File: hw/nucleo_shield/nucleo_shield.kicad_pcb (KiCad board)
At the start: 2 copper layers, 151 x 90.9 mm, 69 parts, among them CN101 Nucleo-F411RE-CN10, CN71 Nucleo-F411RE-CN7, P1 CONN_INH1, P10 CONN_OUTH1, P11 CONN_OUTH2, P12 CONN_RS485_OUT, P13 CONN_RS485_IN, P15 CONN_EXT2, P16 CONN_EXTI2C, P18 CONN_1WIRE, P19 CONN_EXT_SPI, P2 CONN_OUT3, P20 CON_BME, P3 POWER_24V_CON, P4 POWER_CON, P5 CONN_INH2, P6 ETH_CONN, P7 CONN_LCD_SD, P8 CONN_OUT4, P9 CONN_SCT, U1 74HC595, U10 ULN2803, U11 74HC595, U12 74HC595, U14 PCF8574A, U2 74HC595, U3 LTV-847, U4 LTV-847, U5 LTV-847, U6 LTV-847, U7 PCF8574A, U8 PCF8574A, U9 ULN2803

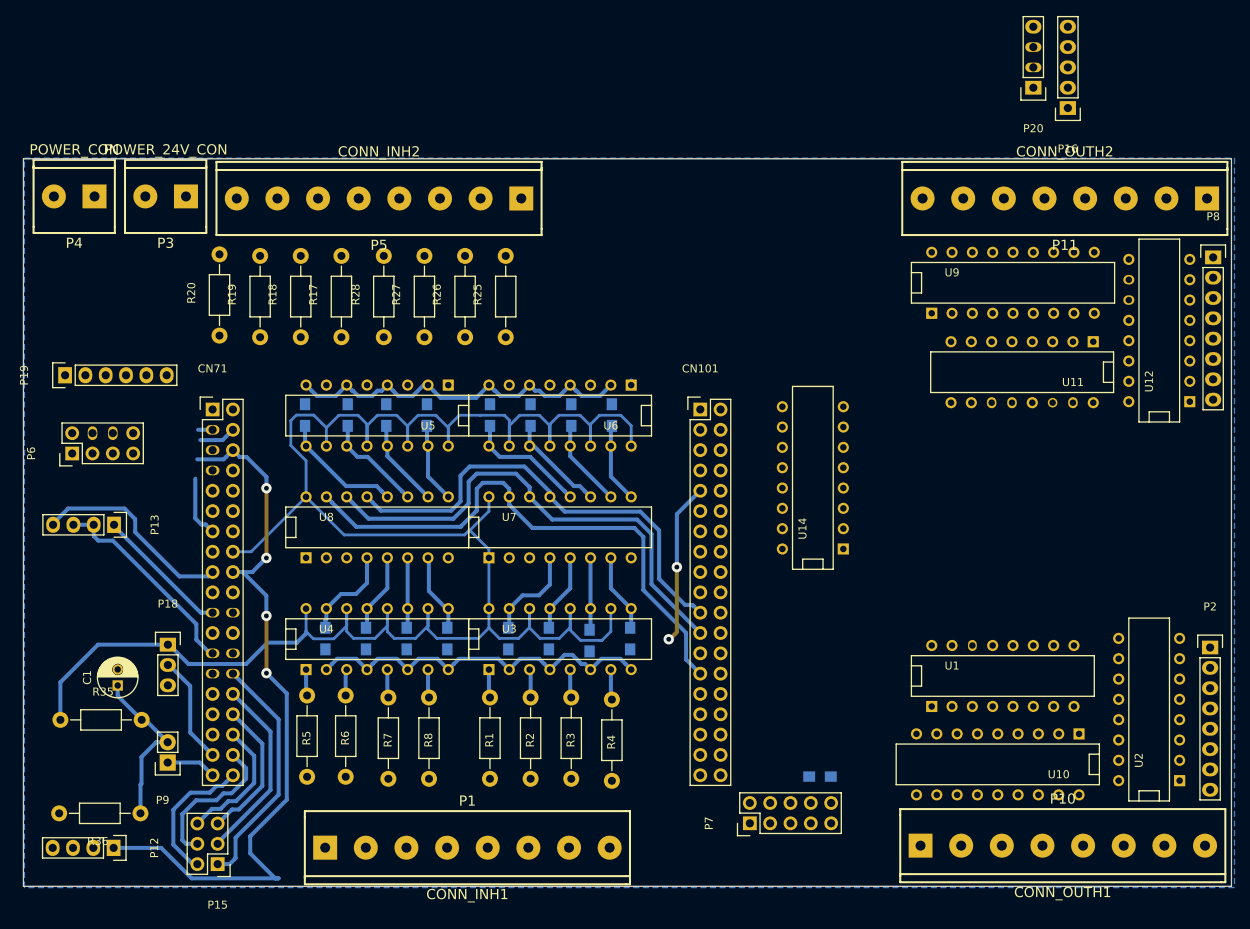
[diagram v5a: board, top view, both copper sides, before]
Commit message: HW: rework of nucleo shield to add more IOs
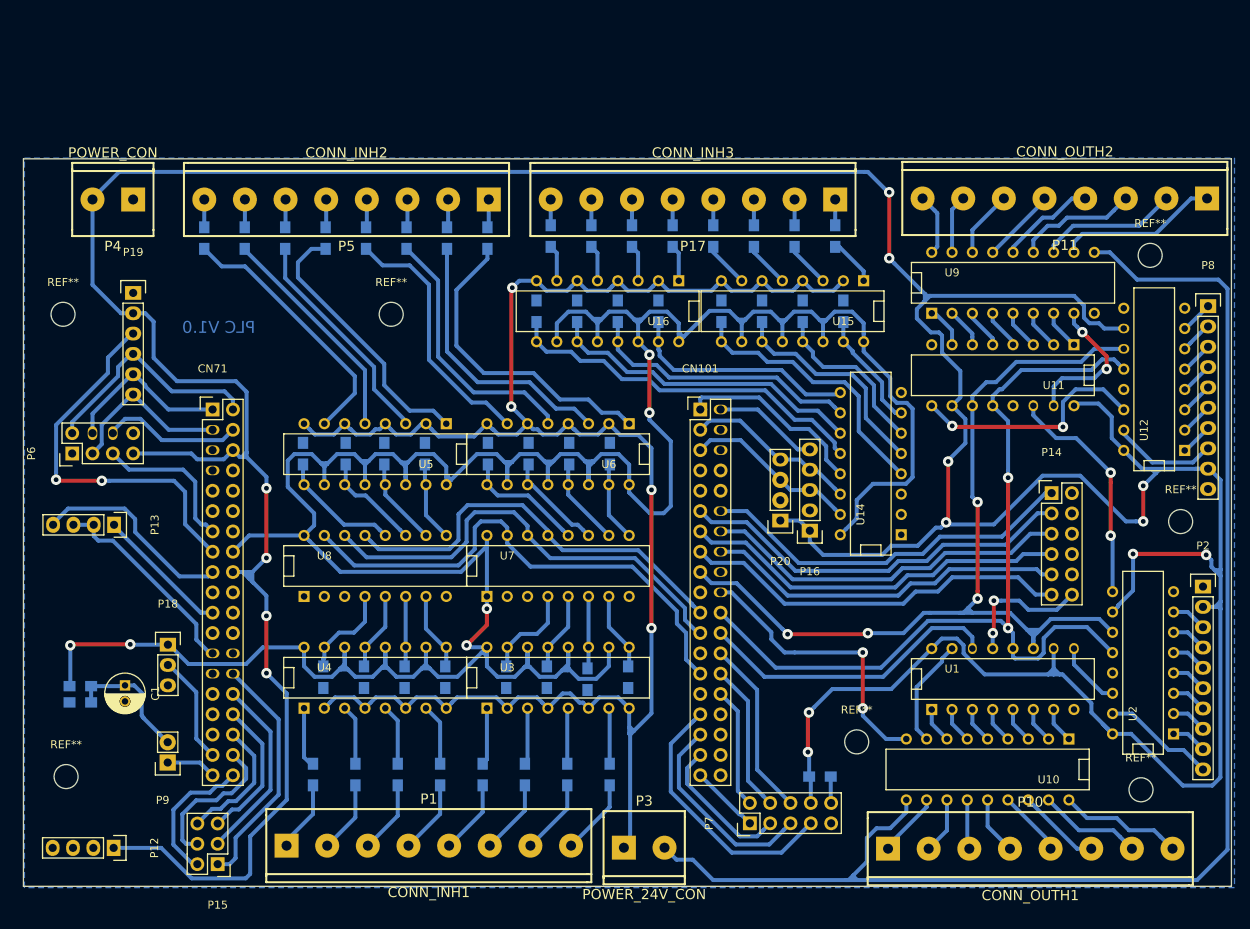
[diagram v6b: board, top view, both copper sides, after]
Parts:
- added P14: CONN_02X06, Pin_Headers:Pin_Header_Straight_2x06, F.Cu at (223.6, 99.8)
- added P17: CONN_INH3, w_conn_screw:mors_8p, F.Cu at (178.8, 63.1)
- added R34: R, Resistors_SMD:R_0805_HandSoldering, B.Cu at (196.6, 67.7)
- added R37: R, Resistors_SMD:R_0805_HandSoldering, B.Cu at (191.5, 67.7)
- added R38: R, Resistors_SMD:R_0805_HandSoldering, B.Cu at (186.4, 67.7)
- added R39: R, Resistors_SMD:R_0805_HandSoldering, B.Cu at (181.4, 67.7)
- added R40: R, Resistors_SMD:R_0805_HandSoldering, B.Cu at (176.3, 67.7)
- added R41: R, Resistors_SMD:R_0805_HandSoldering, B.Cu at (171.2, 67.7)
- added R42: R, Resistors_SMD:R_0805_HandSoldering, B.Cu at (166.1, 67.7)
- added R43: R, Resistors_SMD:R_0805_HandSoldering, B.Cu at (161.0, 67.7)
- added R44: R, Resistors_SMD:R_0805_HandSoldering, B.Cu at (182.4, 77.1)
- added R45: R, Resistors_SMD:R_0805_HandSoldering, B.Cu at (159.3, 77.1)
- added R46: R, Resistors_SMD:R_0805_HandSoldering, B.Cu at (187.5, 77.1)
- added R47: R, Resistors_SMD:R_0805_HandSoldering, B.Cu at (164.3, 77.1)
- added R48: R, Resistors_SMD:R_0805_HandSoldering, B.Cu at (192.5, 77.1)
- added R49: R, Resistors_SMD:R_0805_HandSoldering, B.Cu at (169.4, 77.1)
- added R50: R, Resistors_SMD:R_0805_HandSoldering, B.Cu at (197.6, 77.1)
- added R51: R, Resistors_SMD:R_0805_HandSoldering, B.Cu at (174.5, 77.1)
- added REF**: MountingHole_3mm, Mounting_Holes:MountingHole_3mm, F.Cu at (236.0, 70.1)
- added REF**: MountingHole_3mm, Mounting_Holes:MountingHole_3mm, F.Cu at (100.5, 135.3)
- added REF**: MountingHole_3mm, Mounting_Holes:MountingHole_3mm, F.Cu at (141.1, 77.5)
- added REF**: MountingHole_3mm, Mounting_Holes:MountingHole_3mm, F.Cu at (100.1, 77.5)
- added REF**: MountingHole_3mm, Mounting_Holes:MountingHole_3mm, F.Cu at (239.8, 103.4)
- added REF**: MountingHole_3mm, Mounting_Holes:MountingHole_3mm, F.Cu at (234.8, 136.9)
- added REF**: MountingHole_3mm, Mounting_Holes:MountingHole_3mm, F.Cu at (199.3, 130.9)
- added U15: LTV-847, Housings_DIP:DIP-16__300, F.Cu at (191.3, 77.1)
- added U16: LTV-847, Housings_DIP:DIP-16__300, F.Cu at (168.1, 77.1)
- P2, P8: footprint Pin_Headers:Pin_Header_Straight_1x08 -> Pin_Headers:Pin_Header_Straight_1x10
- R1, R17, R18, R19, R2, R20, R25, R26, R27, R28, R3, R35, R36, R4, R5, R6, R7, R8: footprint Resistors_ThroughHole:Resistor_Horizontal_RM10mm -> Resistors_SMD:R_0805_HandSoldering; moved to B.Cu
- moved P3 101.0 mm to (172.7, 144.1), turned to 0 degrees
- moved P20 62.7 mm to (189.7, 103.3)
- moved P16 61.9 mm to (193.4, 104.5)
- moved R36 15.8 mm to (102.2, 126.0)
- moved P19 13.4 mm to (108.8, 74.8), turned to 0 degrees
- moved R25 12.6 mm to (153.1, 67.9)
- moved R26 12.6 mm to (148.1, 67.9)
- moved R27 12.6 mm to (143.0, 67.9)
- moved R28 12.6 mm to (138.0, 67.9)
- moved P2 7.67 mm to (242.6, 111.5)
- moved R17 7.57 mm to (132.9, 67.9)
- moved R18 7.56 mm to (127.8, 67.9)
- moved R19 7.56 mm to (122.8, 67.9)
- moved U14 7.45 mm to (201.0, 96.1)
- moved R20 7.36 mm to (117.7, 67.9)
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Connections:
- CN101 pad 1: I2C_GPIO -> I2C1_GPIO
- CN101 pad 10: Net-(CN101-Pad10) -> (no net)
- CN101 pad 11: Net-(CN101-Pad11) -> /PA5
- CN101 pad 12: SRLatch2 -> /PA12
- CN101 pad 13: Net-(CN101-Pad13) -> /PA6
- CN101 pad 14: SRDATA2 -> /PA11
- CN101 pad 15: Net-(CN101-Pad15) -> /PA7
- CN101 pad 16: SRCLK -> /PB12
- CN101 pad 17: Net-(CN101-Pad17) -> SRCLK
- CN101 pad 18: Net-(CN101-Pad18) -> (no net)
- CN101 pad 19: Net-(CN101-Pad19) -> (no net)
- CN101 pad 2: I2C1_GPIO -> I2C_GPIO
- CN101 pad 25: Net-(CN101-Pad25) -> (no net)
- CN101 pad 29: Net-(CN101-Pad29) -> (no net)
- CN101 pad 32: Net-(CN101-Pad32) -> (no net)
- CN101 pad 34: Net-(CN101-Pad34) -> (no net)
- CN101 pad 36: Net-(CN101-Pad36) -> (no net)
- CN101 pad 38: Net-(CN101-Pad38) -> (no net)
- CN101 pad 4: Net-(CN101-Pad4) -> (no net)
- CN101 pad 6: SRCLK2 -> (no net)
- CN101 pad 7: Net-(CN101-Pad7) -> (no net)
- CN101 pad 8: Net-(CN101-Pad8) -> (no net)
- CN71 pad 10: Net-(CN71-Pad10) -> (no net)
- CN71 pad 11: Net-(CN71-Pad11) -> (no net)
- CN71 pad 12: Net-(CN71-Pad12) -> (no net)
- CN71 pad 14: Net-(CN71-Pad14) -> (no net)
- CN71 pad 23: Net-(CN71-Pad23) -> (no net)
- CN71 pad 24: Net-(CN71-Pad24) -> (no net)
- CN71 pad 26: Net-(CN71-Pad26) -> (no net)
- CN71 pad 27: Net-(CN71-Pad27) -> (no net)
- CN71 pad 29: Net-(CN71-Pad29) -> (no net)
- CN71 pad 31: Net-(CN71-Pad31) -> (no net)
- CN71 pad 33: Net-(CN71-Pad33) -> (no net)
- CN71 pad 5: +3V3 -> (no net)
- CN71 pad 7: Net-(CN71-Pad7) -> (no net)
- CN71 pad 9: Net-(CN71-Pad9) -> (no net)
- P12 pad 2: Net-(P12-Pad2) -> (no net)
- P12 pad 3: Net-(P12-Pad3) -> (no net)
- P16 pad 3: I2C_GPIO -> I2C1_SDA
- P16 pad 5: I2C1_SDA -> I2C_GPIO
- P2 pad 1: out24 -> GND
- P2 pad 2: out23 -> +5V
- P2 pad 3: out22 -> out24
- P2 pad 4: out21 -> out23
- P2 pad 5: out20 -> out22
- P2 pad 6: out19 -> out21
- P2 pad 7: out18 -> out20
- P2 pad 8: out17 -> out19
- P20 pad 3: I2C1_SCL -> I2C1_SDA
- P20 pad 4: I2C1_SDA -> I2C1_SCL
- P6 pad 8: GND -> (no net)
- U11 pad 11: SRLatch2 -> SRCLK
- U11 pad 12: SRCLK2 -> SRLatch
- U11 pad 14: SRDATA2 -> Net-(U11-Pad14)
- U12 pad 11: SRLatch2 -> SRCLK
- U12 pad 12: SRCLK2 -> SRLatch
- U12 pad 9: Net-(U12-Pad9) -> (no net)
- U14 pad 1: +3V3 -> GND
- U14 pad 10: Net-(U14-Pad10) -> in22
- U14 pad 11: Net-(U14-Pad11) -> in23
- U14 pad 12: Net-(U14-Pad12) -> in24
- U14 pad 4: Net-(U14-Pad4) -> in17
- U14 pad 5: Net-(U14-Pad5) -> in18
- U14 pad 6: Net-(U14-Pad6) -> in19
- U14 pad 7: Net-(U14-Pad7) -> in20
- U14 pad 9: Net-(U14-Pad9) -> in21
- U2 pad 11: Net-(U2-Pad11) -> SRCLK
- U2 pad 12: Net-(U2-Pad12) -> SRLatch
- U2 pad 9: Net-(U2-Pad9) -> Net-(U11-Pad14)
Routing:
- net +5V: track 92.0 -> 555.6 mm, vias 4 -> 14
- net +24V: track 0.00 -> 177.4 mm
- net +3V3: track 266.5 -> 406.9 mm, vias 0 -> 6
- net GND_24V: track 92.5 -> 221.4 mm, vias 0 -> 4
- net SRCLK: track 0.00 -> 115.3 mm, vias 0 -> 4
- net SRLatch: track 0.00 -> 110.9 mm, vias 0 -> 2
- net /PA5: track 0.00 -> 49.9 mm
- net /PA7: track 0.00 -> 48.9 mm
- net /PA6: track 0.00 -> 48.5 mm
- net EXT_SPI_SS: track 0.00 -> 48.0 mm, vias 0 -> 2
- net /PA12: track 0.00 -> 47.7 mm
- net in24: track 0.00 -> 46.6 mm
- net /PA11: track 0.00 -> 46.2 mm
- net /PB12: track 0.00 -> 45.3 mm
- net in23: track 0.00 -> 40.1 mm
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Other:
- board text added: "PLC V1.0"

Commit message: HW: add another header for i2c
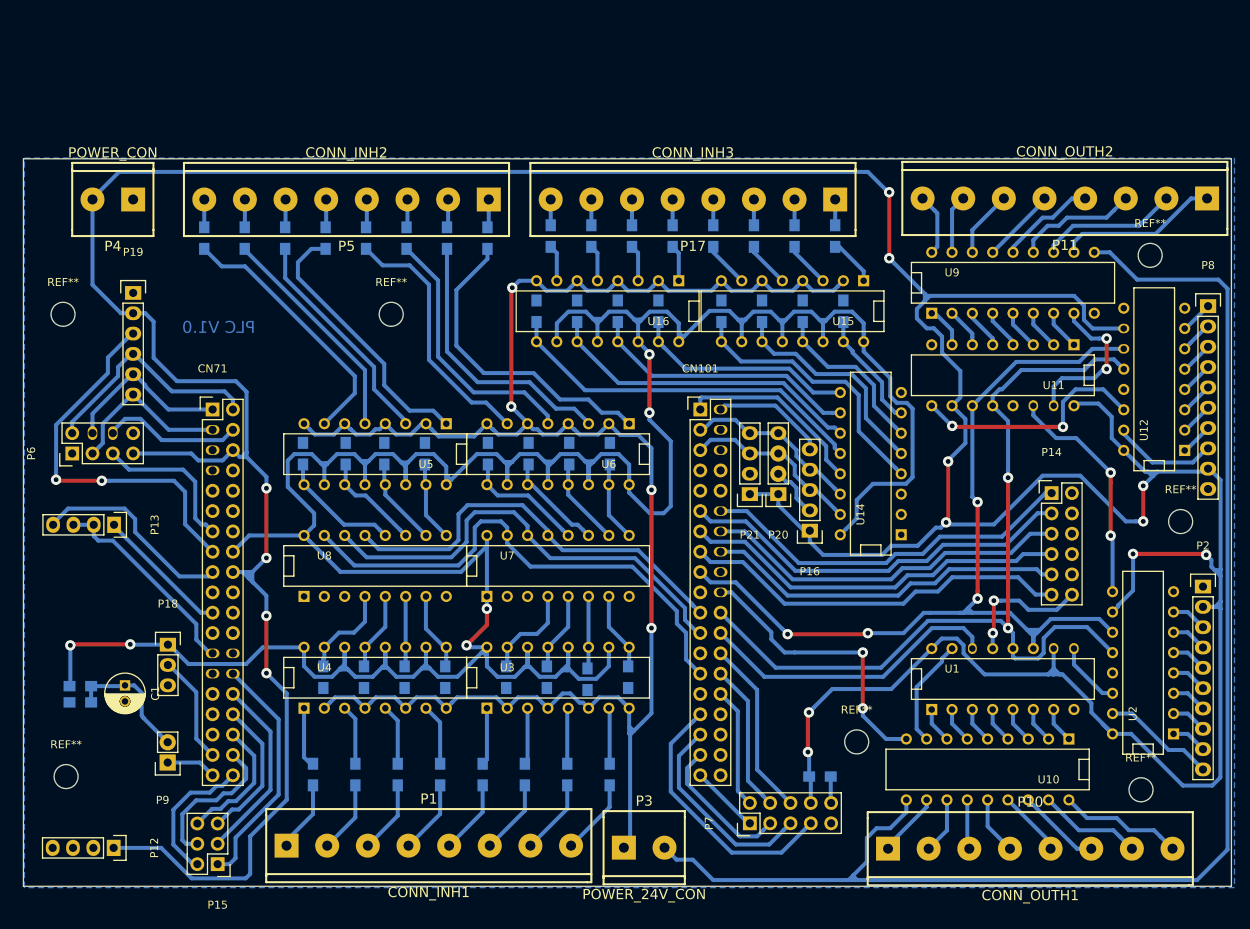
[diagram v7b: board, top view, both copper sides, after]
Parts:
- added P21: CON_BH, Pin_Headers:Pin_Header_Straight_1x04, F.Cu at (185.9, 99.9)
- moved P20 3.31 mm to (189.5, 99.9)
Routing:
- net GND: track 53.2 -> 59.8 mm
- net +5V: track 555.6 -> 561.7 mm
- net in21: track 29.0 -> 27.8 mm
- net out9: track 18.6 -> 19.7 mm
- net I2C_GPIO: track 13.2 -> 14.3 mm
- net I2C1_SDA: track 21.9 -> 22.7 mm
- net SRCLK: track 115.3 -> 114.6 mm
- net in22: track 34.5 -> 34.0 mm
- net I2C1_SCL: track 22.1 -> 22.7 mm
